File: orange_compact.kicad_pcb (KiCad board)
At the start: 6 copper layers, 50 x 45 mm, 222 parts, among them IC1 MCP25625-E_ML, IC3 MIC5317-1.8YD5-TR, IC4 MAX13487EESA+T, IC5 CD4060BPWR, J2 Conn_Coaxial, J3 Conn_Coaxial, J5 Conn_01x08_Pin, J6 USB_B_Micro, Q10 MMBT3904, Q11 MMBT3904, Q12 MMBT3904, Q13 MMBT3904, Q14 MMBT3904, Q3 MMBT3904, Q4 MMBT3904, Q5 MMBT3904, Q6 BC846A,215, Q7 BC846A,215, Q8 MMBT3904, Q9 MMBT3904, U1 EG9xQ, U12 LM3671MF-3.3/NOPB, U13 LIS2DH12TR, U19 MX25R6435FZNIL0, U2 MDBT50Q-1M, U20 TPS566242DRLR, U3 FDMC86139P, U4 LM5012DDAR, U5 TXB0108DQSR, U8 1NCE IoT SIMs Chip, U9 USBLC6-2SC6, Y2 16MHz

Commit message: middle of routing savepoint
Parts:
- removed D20: PESD3V3L1BA-N, Diode_SMD:D_SOD-323
- moved JP1 6.31 mm to (115.5, 68.7)
- moved C59 6.18 mm to (127.2, 62.8)
- moved C55 6.16 mm to (127.6, 66.9), turned to 90 degrees
- moved FID1 5.63 mm to (120.2, 66.0)
- moved R34 5.54 mm to (134.3, 68.6), turned to 0 degrees
- moved Y2 4.58 mm to (141.1, 66.1), turned to -90 degrees
- moved R52 4.09 mm to (127.2, 63.8)
- moved C5 4.04 mm to (138.6, 65.0), turned to 90 degrees
- moved R64 2.71 mm to (115.0, 72.4)
- moved C45 2.60 mm to (149.4, 62.5), turned to 0 degrees
- moved IC5 2.44 mm to (132.2, 65.1), turned to 180 degrees
- moved R2 2.12 mm to (127.2, 64.9)
- moved C27 1.88 mm to (144.4, 91.0)
- moved C28 1.85 mm to (144.4, 92.6)
- moved C10 1.24 mm to (138.6, 67.0), turned to -90 degrees
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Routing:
- net 3V3_ALWAYS_ON: track 1.90 -> 120.8 mm, vias 0 -> 8
- net 5V0: track 0.00 -> 65.6 mm, vias 0 -> 12
- net 4V0: track 0.00 -> 61.9 mm, vias 0 -> 14
- net /RS485_RX: track 0.00 -> 41.9 mm, vias 0 -> 3
- net /CAN_SCK: track 0.00 -> 35.4 mm, vias 0 -> 4
- net /CAN_MOSI: track 0.00 -> 30.8 mm, vias 0 -> 4
- net /CAN_MISO: track 0.00 -> 25.5 mm, vias 0 -> 4
- net /CTS_1V8: track 0.00 -> 21.2 mm, vias 0 -> 3
- net /MODEM_TX_1V8: track 0.00 -> 20.5 mm, vias 0 -> 1
- net /MODEM_RX_1V8: track 0.00 -> 18.5 mm, vias 0 -> 1
- net /RTS_1V8: track 0.00 -> 17.1 mm, vias 0 -> 2
- net /SIM_VDD: track 0.00 -> 15.4 mm, vias 0 -> 2
- net /DCD_1V8: track 0.00 -> 15.1 mm, vias 0 -> 2
- net +1V8: track 0.00 -> 13.1 mm, vias 0 -> 1
- net /SDA: track 0.00 -> 11.8 mm
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- added copper zone on In2.Cu, net 4V0

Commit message: saved route progress 80%
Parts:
- removed C57: 100nF, Capacitor_SMD:C_0402_1005Metric
- moved TP12 22.5 mm to (117.7, 70.0)
- moved C7 1.05 mm to (143.3, 73.6)
- moved C71 0.25 mm to (146.5, 97.2), turned to 90 degrees
- moved R6 0.16 mm to (136.2, 78.5)
- moved C41 0.15 mm to (138.6, 78.7)
- moved R43 0.15 mm to (116.2, 70.6)
- moved R35 0.06 mm to (114.8, 88.8)
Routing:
- net /EBL: track 0.00 -> 58.3 mm, vias 0 -> 2
- net VDD_EXT: track 0.00 -> 57.4 mm, vias 0 -> 2
- net /UART_RS485_RE_SHDN: track 3.69 -> 52.6 mm, vias 1 -> 2
- net /RS485_TX: track 6.95 -> 55.1 mm
- net /GNSS_EN_3V3: track 1.29 -> 48.5 mm, vias 1 -> 3
- net /GNSS_RXD_3V3: track 0.27 -> 46.9 mm, vias 1 -> 2
- net /GNSS_TXD_3V3: track 1.30 -> 42.2 mm, vias 1 -> 2
- net /U20_EN: track 0.00 -> 37.7 mm, vias 0 -> 2
- net /MODEM_DTR_1V8: track 1.70 -> 37.4 mm, vias 1 -> 4
- net /USB_BOOT: track 0.00 -> 32.0 mm, vias 0 -> 4
- net /GNSS_EN_1V8: track 0.00 -> 29.8 mm, vias 0 -> 2
- net Net-(U1-PSM_INT): track 0.00 -> 27.3 mm, vias 0 -> 2
- net /GNSS_RST_3V3: track 1.22 -> 27.0 mm, vias 1 -> 2
- net /STATUS_LED: track 1.70 -> 27.4 mm, vias 1 -> 3
- net /WDI: track 0.00 -> 23.7 mm, vias 0 -> 2
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
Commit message: ready for review
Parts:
- added C1: 10uF, Capacitor_SMD:C_0603_1608Metric, F.Cu at (133.5, 71.3)
- C71: footprint Capacitor_SMD:C_0603_1608Metric -> Capacitor_SMD:C_0402_1005Metric; moved to F.Cu
- CP4, CP5: value T520C107M010ATE025 -> 100u
- D11: moved to F.Cu
- IC5: value CD4060BPWR -> MC74HC4060A
- R2: value 220k -> 1M
- moved C71 18.0 mm to (129.2, 92.1)
- moved D11 17.2 mm to (127.0, 92.1), turned to 0 degrees
- moved C26 11.6 mm to (138.5, 103.5)
- moved C60 6.67 mm to (131.6, 72.0)
- moved TP12 3.05 mm to (115.3, 68.0)
- moved CP5 1.64 mm to (131.2, 65.1)
- moved TP10 1.13 mm to (149.9, 98.5)
- moved Q13 1.13 mm to (160.4, 94.9)
- moved D21 1.12 mm to (160.8, 100.0)
- moved R72 1.11 mm to (160.8, 98.4)
- moved R19 1.10 mm to (138.1, 101.2)
- moved C85 0.96 mm to (136.3, 64.1)
- moved C87 0.96 mm to (136.3, 66.3)
- moved C86 0.96 mm to (136.3, 65.2)
- moved TP11 0.58 mm to (149.4, 96.5)
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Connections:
- C15 pad 1: 1V8 -> VDD_EXT
- IC5 pad 2: /WDO -> unconnected-(IC5-Q13-Pad2)
- IC5 pad 3: unconnected-(IC5-Q14-Pad3) -> /WDO
- U5 pad 5: 1V8 -> VDD_EXT
- U5 pad 6: 1V8 -> VDD_EXT
- U8 pad 1: /SIM_VDD -> GND
- U8 pad 2: /SIM_RST -> unconnected-(U8-VPP-Pad2)
- U8 pad 3: /SIM_CLK -> /SIM_DATA
- U8 pad 5: GND -> unconnected-(U8-C4-Pad5)
- U8 pad 6: unconnected-(U8-VPP-Pad6) -> /SIM_CLK
- U8 pad 7: /SIM_DATA -> /SIM_RST
- U8 pad 8: unconnected-(U8-C8-Pad8) -> /SIM_VDD
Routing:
- net +1V8: track 13.1 -> 92.4 mm, vias 1 -> 3
- net 5V0: track 84.5 -> 146.2 mm, vias 13 -> 28
- net /WDO: track 0.00 -> 57.8 mm, vias 0 -> 2
- net Net-(D21-A): track 0.00 -> 55.1 mm, vias 0 -> 3
- net 3V3_ALWAYS_ON: track 134.0 -> 179.7 mm, vias 9 -> 15
- net /PWRKEY: track 0.00 -> 22.8 mm, vias 0 -> 2
- net VDD_EXT: track 57.4 -> 79.7 mm, vias 2 -> 4
- net Net-(D8-A2): track 0.00 -> 20.9 mm
- net /AUX_LED: track 2.37 -> 22.5 mm
- net /NRF_LED: track 0.00 -> 19.8 mm, vias 0 -> 2
- net /EBL: track 58.3 -> 76.7 mm, vias 2 -> 4
- net Net-(Q5-B): track 0.00 -> 16.3 mm, vias 0 -> 2
- net Net-(D6-K): track 0.00 -> 16.1 mm
- net Net-(Q5-C): track 0.00 -> 15.6 mm
- net VIN: track 0.00 -> 14.1 mm, vias 0 -> 12
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- added copper zone on F.Cu, net 3V3_ALWAYS_ON
- added copper zone on In2.Cu, net 3V3_ALWAYS_ON
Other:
- board text added: "CH"
- board text added: "CL"
- board text added: "CON"
- board text added: "D+"
- board text added: "D-"
- board text added: "G"
- board text added: "NET"
- board text added: "ORANGE LIGHT EG916 P1"
- board text added: "PPS"
- board text added: "PSM"
- board text added: "PWR"
- board text added: "SC"
- board text added: "SD"
- board text removed: "GNNS BU"

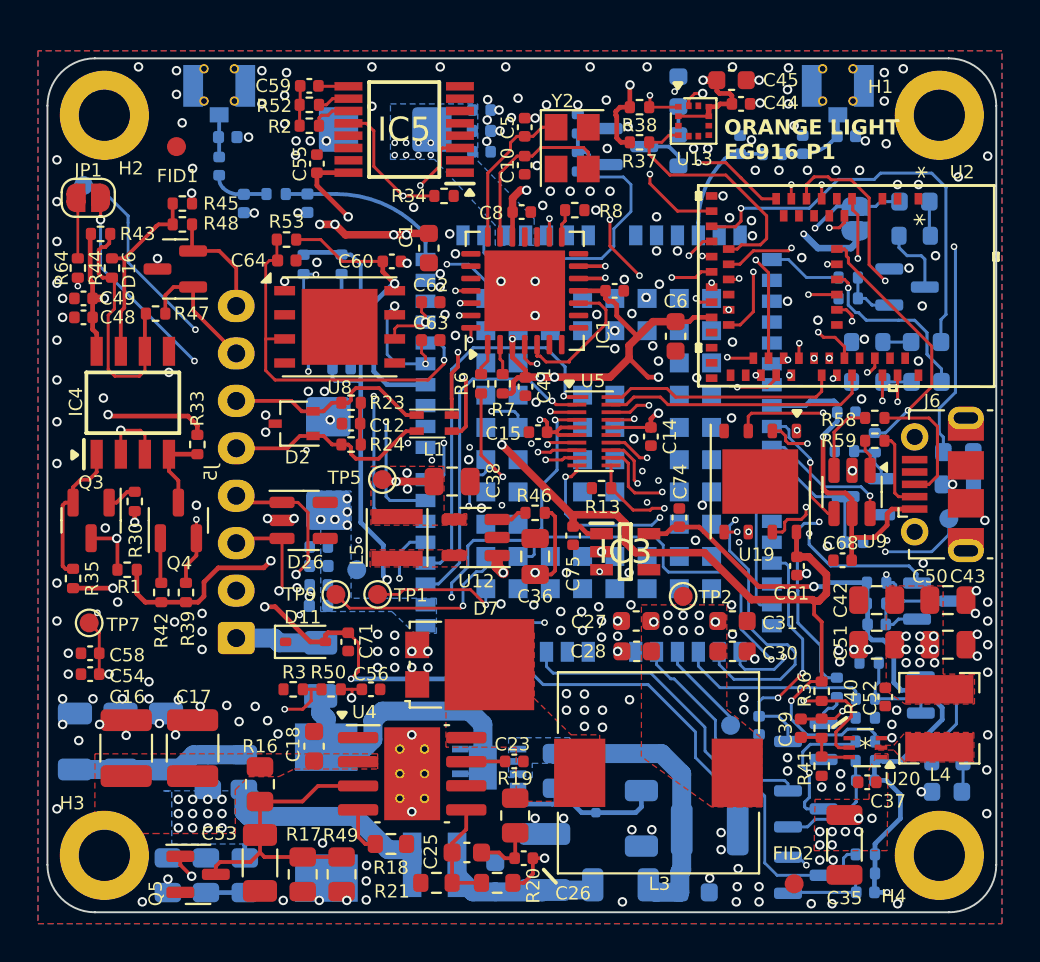
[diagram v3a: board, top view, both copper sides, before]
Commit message: Added gnss power
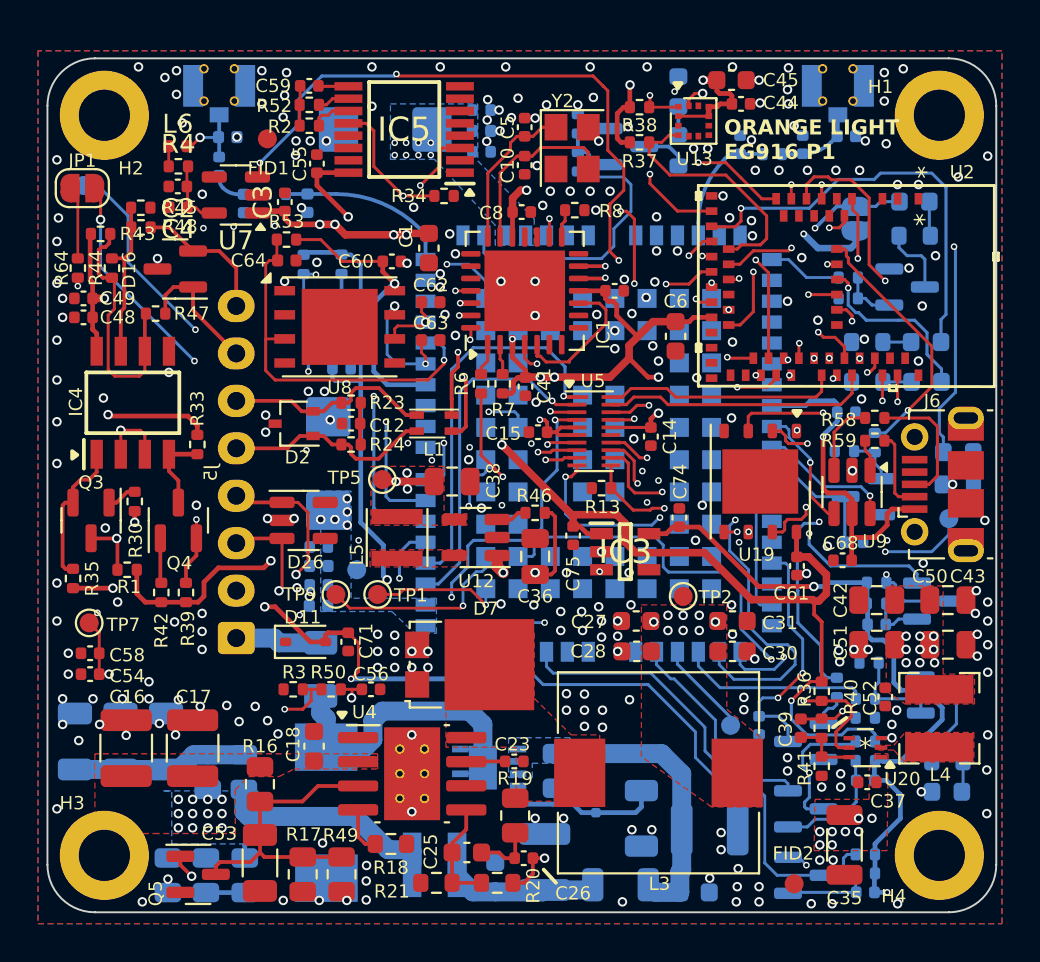
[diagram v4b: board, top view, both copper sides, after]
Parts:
- added C2: 100pf, Capacitor_SMD:C_0402_1005Metric, F.Cu at (120.3, 68.1)
- added C3: 2.2uF, Capacitor_SMD:C_0402_1005Metric, F.Cu at (125.9, 68.9)
- added C4: 1uF, Capacitor_SMD:C_0402_1005Metric, F.Cu at (120.3, 69.2)
- added L6: 51nH, Inductor_SMD:L_0402_1005Metric, F.Cu at (120.3, 66.0)
- added R4: 10, Resistor_SMD:R_0402_1005Metric, F.Cu at (120.3, 67.0)
- added U7: LP5907MFX-3.3, Package_TO_SOT_SMD:SOT-23-5, F.Cu at (123.3, 68.5)
- C116: value 33nF -> 24pf
- IC3: footprint MIC5317:SOT95P280X130-5N -> TC-ICs:SOT95P280X130-5N
- IC5: footprint CD4060BPWR:SOP65P640X120-16N -> TC-ICs:SOP65P640X120-16N
- moved FID1 4.81 mm to (125.0, 65.6)
- moved R45 2.20 mm to (118.3, 69.2)
- moved R48 2.19 mm to (118.3, 70.3)
- moved JP1 0.60 mm to (115.2, 68.2)
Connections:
- U2 pad 49: unconnected-(U2-P0.25-Pad49) -> /GPS_ANT_EN
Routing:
- net /GPS_ANT_EN: track 0.00 -> 47.1 mm, vias 0 -> 4
- net 5V0: track 146.2 -> 150.1 mm
- net 3V3_ANT: track 0.00 -> 3.73 mm
- net Net-(D13-A2): track 2.25 -> 4.11 mm, vias 0 -> 1
- net Net-(IC4-B): track 10.1 -> 8.46 mm
- net /D-/B: track 6.07 -> 7.40 mm
- net /USB_BOOT: track 32.3 -> 33.5 mm
- net Net-(L6-Pad1): track 0.00 -> 1.06 mm
- net Net-(IC1-TXCAN): track 16.9 -> 17.8 mm
- net Net-(JP1-A): track 3.23 -> 3.87 mm
- net GND: vias 264 -> 266

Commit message: ready to order
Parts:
- moved R53 0.09 mm to (126.0, 71.0)
- moved C4 0.06 mm to (120.2, 69.2)
